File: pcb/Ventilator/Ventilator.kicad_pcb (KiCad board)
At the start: 2 copper layers, 103 x 86.5 mm, 79 parts, among them J1 Conn_02x03_Top_Bottom, J2 Screw_Terminal_01x08, J4 Screw_Terminal_01x02, K1 FINDER-40.52.7.012.0000, K2 FINDER-40.52.7.012.0000, Q1 NUD3160, Q2 NUD3160, Q3 NUD3160, SW1 Reset, U1 Pico, U2 4N25, U3 4N25, U4 4N25, U5 4N25

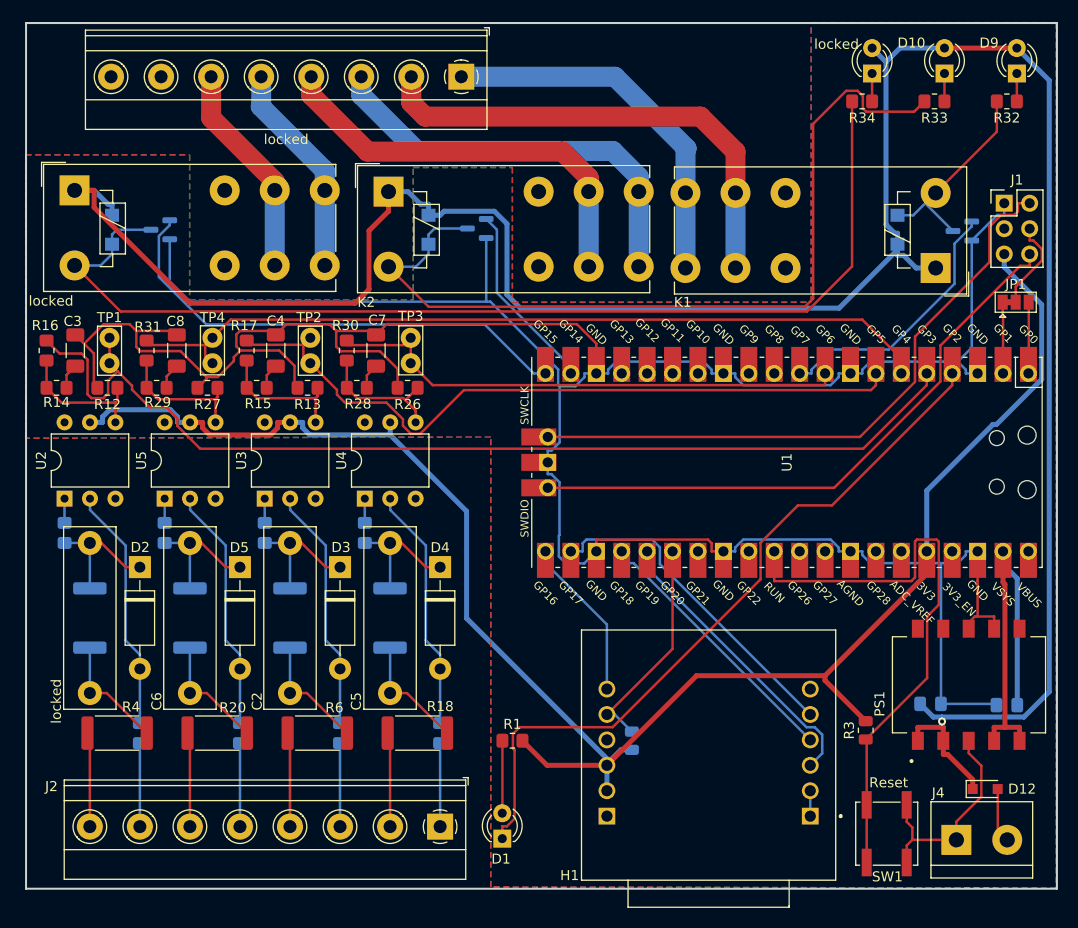
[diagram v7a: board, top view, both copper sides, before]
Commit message: -Ventcontrol 1.2 (routed)
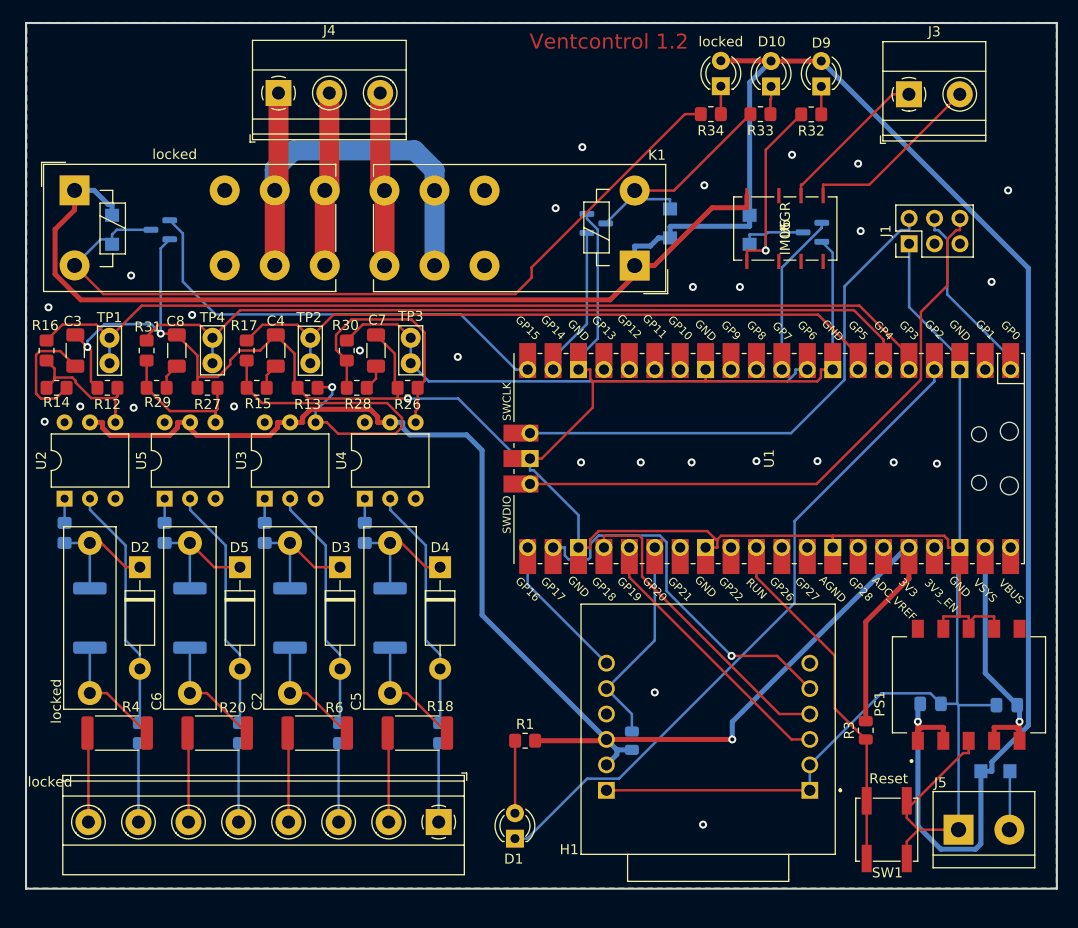
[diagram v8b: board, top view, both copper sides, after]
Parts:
- removed JP1: SolderJumper_3_Bridged12, Jumper:SolderJumper-3_P1.3mm_Bridged12_Pad1.0x1.5mm
- removed the K1 at (127.9, 125.0)
- removed the locked at (80.5, 105.9)
- added J3: Screw_Terminal_01x02, TerminalBlock_Phoenix:TerminalBlock_Phoenix_MKDS-1,5-2-5.08_1x02_P5.08mm_Horizontal, F.Cu at (125.2, 107.6)
- added J4: Screw_Terminal_01x03, TerminalBlock_Phoenix:TerminalBlock_Phoenix_MKDS-1,5-3-5.08_1x03_P5.08mm_Horizontal, F.Cu at (62.2, 107.5)
- added U6: IM06GR, IM06GR:IM06GR, F.Cu at (112.9, 121.0)
- D12: footprint Diode_SMD:D_SOD-323_HandSoldering -> Diode_SMD:D_SMF; moved to B.Cu
- moved K1 25.7 mm to (97.8, 124.7), turned to 180 degrees
- moved D7 24.1 mm to (101.3, 120.5), turned to 90 degrees
- moved D9 19.6 mm to (116.5, 106.8)
- moved R32 19.6 mm to (115.5, 109.6)
- moved R33 17.4 mm to (110.4, 109.6)
- moved D10 17.4 mm to (111.4, 106.8)
- moved R34 15.2 mm to (105.4, 109.6)
- moved locked 15.2 mm to (106.4, 106.8)
- moved Q1 15.0 mm to (115.6, 121.4)
- moved D6 14.8 mm to (109.3, 121.2), turned to -90 degrees
- moved Q2 11.9 mm to (94.0, 120.5), turned to 0 degrees
- moved J1 10.3 mm to (125.2, 122.6), turned to 90 degrees
- moved H1 2.59 mm to (105.5, 172.4)
- moved D12 2.05 mm to (133.9, 175.3)
- moved U1 1.82 mm to (111.3, 144.0)
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- renumbered J4 to J5, K2 to K1, J2 to locked
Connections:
- J1 pad 5: +3.3V -> Net-(J1-Pad5)
- U1 pad 1: Net-(JP1-Pad3) -> /CPU/RX
- U1 pad 2: Net-(JP1-Pad1) -> unconnected-(U1-Pad2)
- locked pad 11: /Output/220_6 -> /Output/220_4
- locked pad 21: /Output/220_6 -> /Output/220_4
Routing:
- net Net-(D7-Pad2): track 87.0 -> 24.1 mm
- net /Output/220_2: track 48.6 -> 0.00 mm
- net /Output/220_1: track 37.5 -> 0.00 mm
- net Net-(D8-Pad2): track 108.2 -> 81.7 mm
- net +3.3V: track 177.0 -> 150.5 mm, vias 0 -> 1
- net /Output/220_3: track 42.0 -> 17.4 mm
- net Net-(R3-Pad1): track 58.4 -> 35.6 mm
- net Net-(R13-Pad1): track 13.6 -> 35.5 mm, vias 0 -> 1
- net /Output/220_6: track 21.5 -> 0.00 mm
- net Net-(J3-Pad2): track 0.00 -> 18.5 mm
- net Net-(J3-Pad1): track 0.00 -> 15.6 mm
- net +5V: track 38.9 -> 25.0 mm, vias 0 -> 1
- net GND: track 335.8 -> 348.8 mm, vias 0 -> 31
- net Net-(R26-Pad1): track 13.5 -> 25.1 mm
- net /CPU/IN1: track 105.6 -> 94.7 mm
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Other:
- board text added: "Ventcontrol 1.2"
